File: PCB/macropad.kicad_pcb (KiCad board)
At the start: 2 copper layers, 83.5 x 97.3 mm, 40 parts, among them SW1 SW_Push, SW10 SW_Push, SW11 SW_Push, SW12 SW_Push, SW13 SW_Push, SW14 SW_Push, SW15 SW_Push, SW16 SW_Push, SW2 SW_Push, SW3 SW_Push, SW4 SW_Push, SW5 SW_Push, SW6 SW_Push, SW7 SW_Push, SW8 SW_Push, SW9 SW_Push, U2 MOUDLE-SEEEDUINO-XIAO

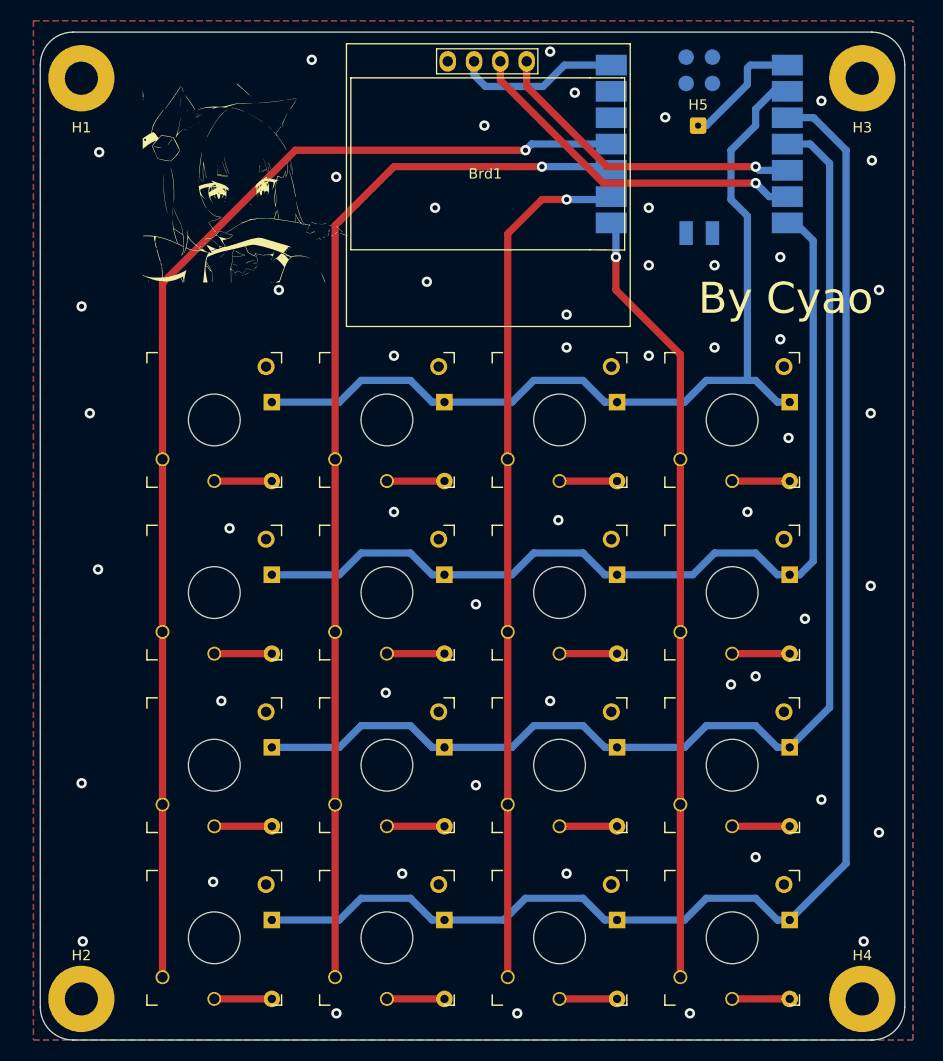
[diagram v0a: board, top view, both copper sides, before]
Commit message: Add pullup resistors for I2C
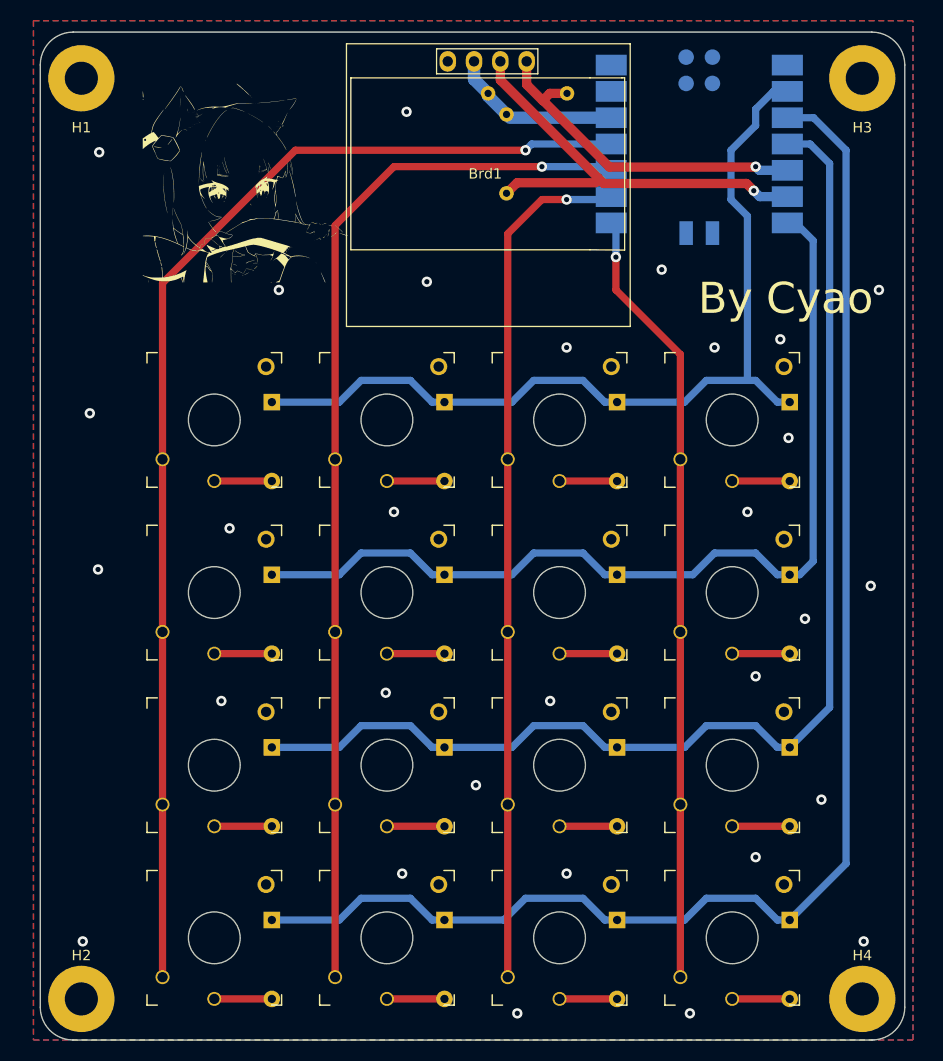
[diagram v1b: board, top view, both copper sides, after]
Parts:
- removed H5: MountingHole_Pad, Connector_Wire:SolderWire-0.1sqmm_1x01_D0.4mm_OD1mm
- added R1: R4.7, Resistor_THT:R_Axial_DIN0204_L3.6mm_D1.6mm_P7.62mm_Horizontal, B.Cu at (151.4, 57.5)
- added R2: R4.7, Resistor_THT:R_Axial_DIN0204_L3.6mm_D1.6mm_P7.62mm_Horizontal, B.Cu at (149.6, 55.4)
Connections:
- Brd1 pad 2: +5V -> +3.3V
- U2 pad 1: Net-(U2-PA02_A0_D0) -> unconnected-(U2-PA02_A0_D0-Pad1)
- U2 pad 12: +3V3 -> +3.3V
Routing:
- net +3.3V: track 0.00 -> 16.7 mm
- net +5V: track 15.9 -> 0.00 mm
- net Net-(U2-PA02_A0_D0): track 12.0 -> 0.00 mm
- net Net-(Brd1-SCL): track 34.6 -> 44.0 mm
- net Net-(Brd1-SDA): track 31.2 -> 33.7 mm
- net GND: vias 53 -> 30

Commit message: Moved diodes
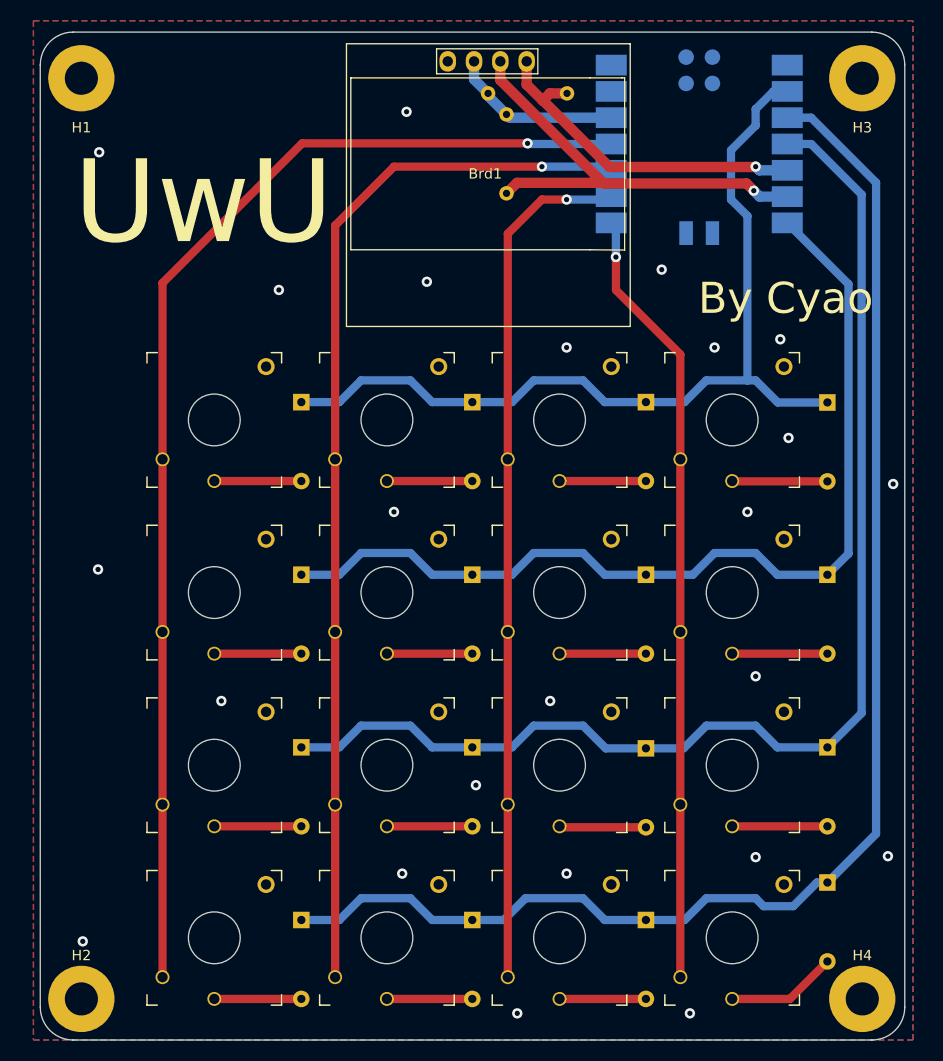
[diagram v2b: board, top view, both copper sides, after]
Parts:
- removed Gura!: LOGO, LOGO
- moved D13 5.13 mm to (182.4, 131.6)
- moved D10 3.64 mm to (182.4, 85.3)
- moved D11 3.64 mm to (182.4, 101.9)
- moved D12 3.64 mm to (182.4, 118.6)
- moved D1 2.85 mm to (131.6, 85.2)
- moved D16 2.85 mm to (131.6, 135.3)
- moved D4 2.85 mm to (131.6, 101.9)
- moved D7 2.85 mm to (131.6, 118.6)
- moved D9 2.79 mm to (164.8, 118.7)
- moved D14 2.78 mm to (164.8, 135.3)
- moved D3 2.78 mm to (164.8, 85.2)
- moved D6 2.78 mm to (164.8, 101.9)
- moved D15 2.69 mm to (148.1, 135.3)
- moved D2 2.69 mm to (148.1, 85.2)
- moved D5 2.69 mm to (148.1, 101.9)
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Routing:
- net Net-(D13-A): track 5.56 -> 10.7 mm
- net Net-(D10-A): track 5.56 -> 9.21 mm
- net Net-(D12-A): track 5.56 -> 9.20 mm
- net Net-(D11-A): track 5.56 -> 9.20 mm
- net Net-(D7-A): track 5.56 -> 8.40 mm
- net Net-(D4-A): track 5.56 -> 8.40 mm
- net Net-(D16-A): track 5.56 -> 8.40 mm
- net Net-(D1-A): track 5.56 -> 8.40 mm
- net Net-(D9-A): track 5.56 -> 8.38 mm
- net Net-(D6-A): track 5.56 -> 8.34 mm
- net Net-(D3-A): track 5.56 -> 8.34 mm
- net Net-(D14-A): track 5.56 -> 8.34 mm
- net Net-(D8-A): track 5.56 -> 8.25 mm
- net Net-(D5-A): track 5.56 -> 8.25 mm
- net Net-(D2-A): track 5.56 -> 8.25 mm
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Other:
- board text added: "UwU"

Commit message: Change side of tracks connecting to keys
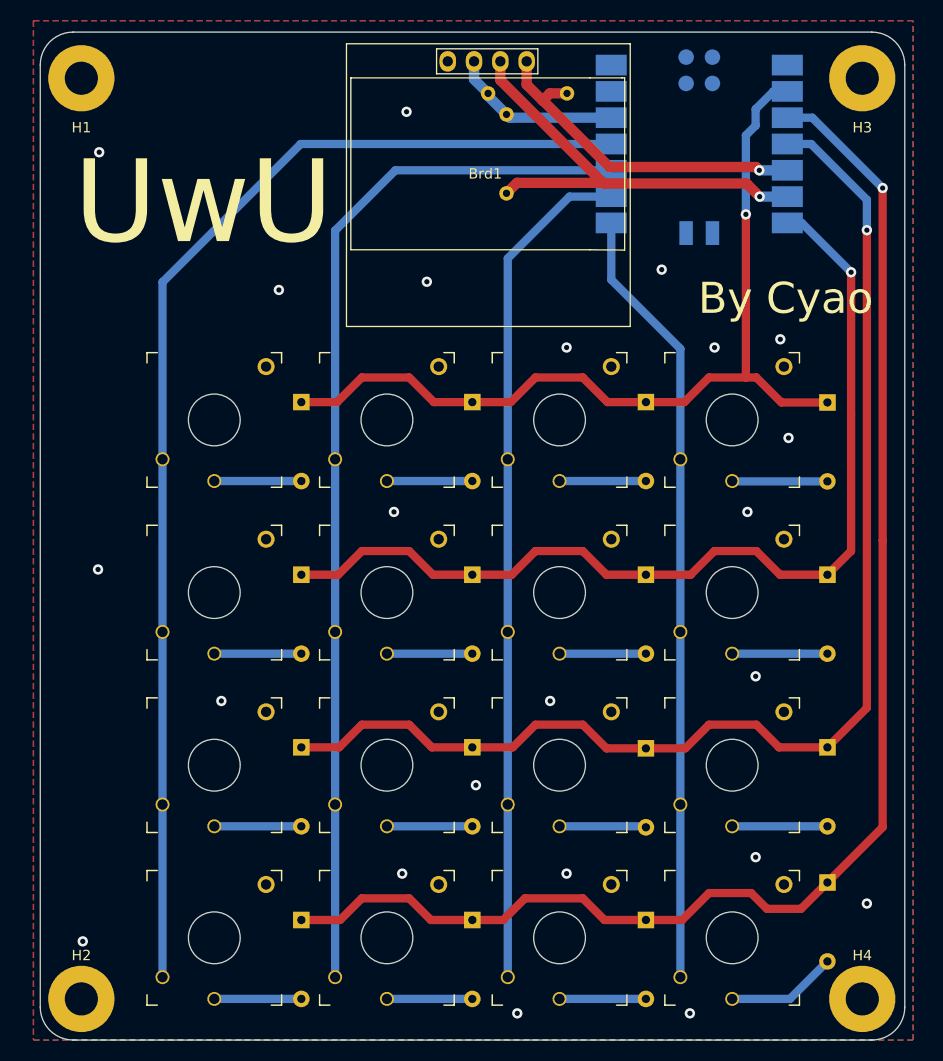
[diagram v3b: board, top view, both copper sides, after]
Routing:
- net ROW3: track 137.1 -> 138.3 mm, vias 0 -> 1
- net COL2: track 83.3 -> 82.3 mm, vias 1 -> 0
- net ROW0: track 87.6 -> 86.8 mm, vias 0 -> 1
- net ROW1: track 94.1 -> 94.8 mm, vias 0 -> 1
- net ROW2: track 120.0 -> 120.7 mm, vias 0 -> 1
- net COL3: track 75.6 -> 76.2 mm, vias 1 -> 0
- net COL1: vias 1 -> 0
- net COL0: vias 1 -> 0
- net GND: vias 24 -> 23

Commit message: Misc improvements
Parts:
- D1, D10, D11, D12, D13, D14, D15, D16, D2, D3, D4, D5, D6, D7, D8, D9: value D -> Didode 1N4148
- H1, H2, H3, H4: value MountingHole_Pad -> Mounting Hole
- R1, R2: value R4.7 -> Resistor 4.7k ohm
- SW1, SW10, SW11, SW12, SW13, SW14, SW15, SW16, SW2, SW3, SW4, SW5, SW6, SW7, SW8, SW9: value SW_Push -> Kailh Choc V2
- U2: value MOUDLE-SEEEDUINO-XIAO -> SEEEDUINO XIAO RP2040
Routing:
- net GND: vias 23 -> 22
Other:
- board text removed: "UwU"

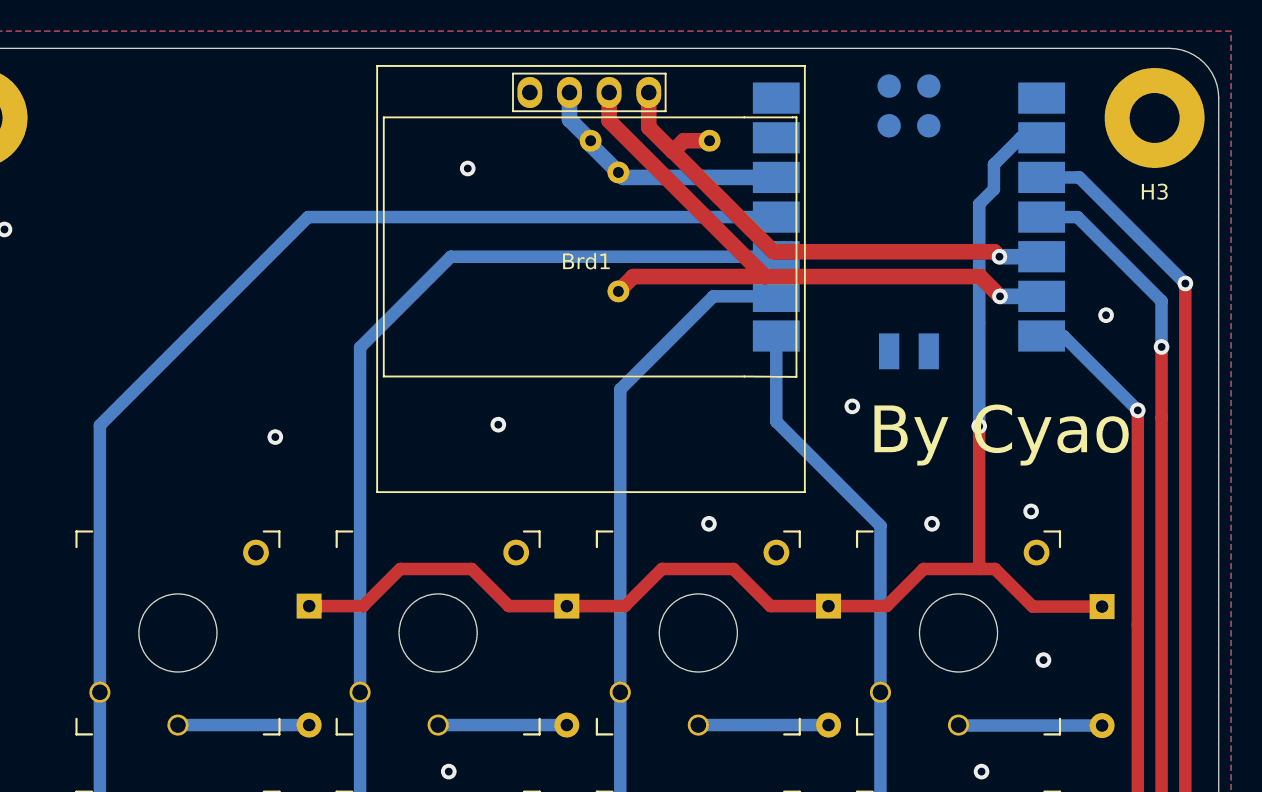
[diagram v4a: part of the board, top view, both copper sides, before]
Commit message: Use thru-hole xiao
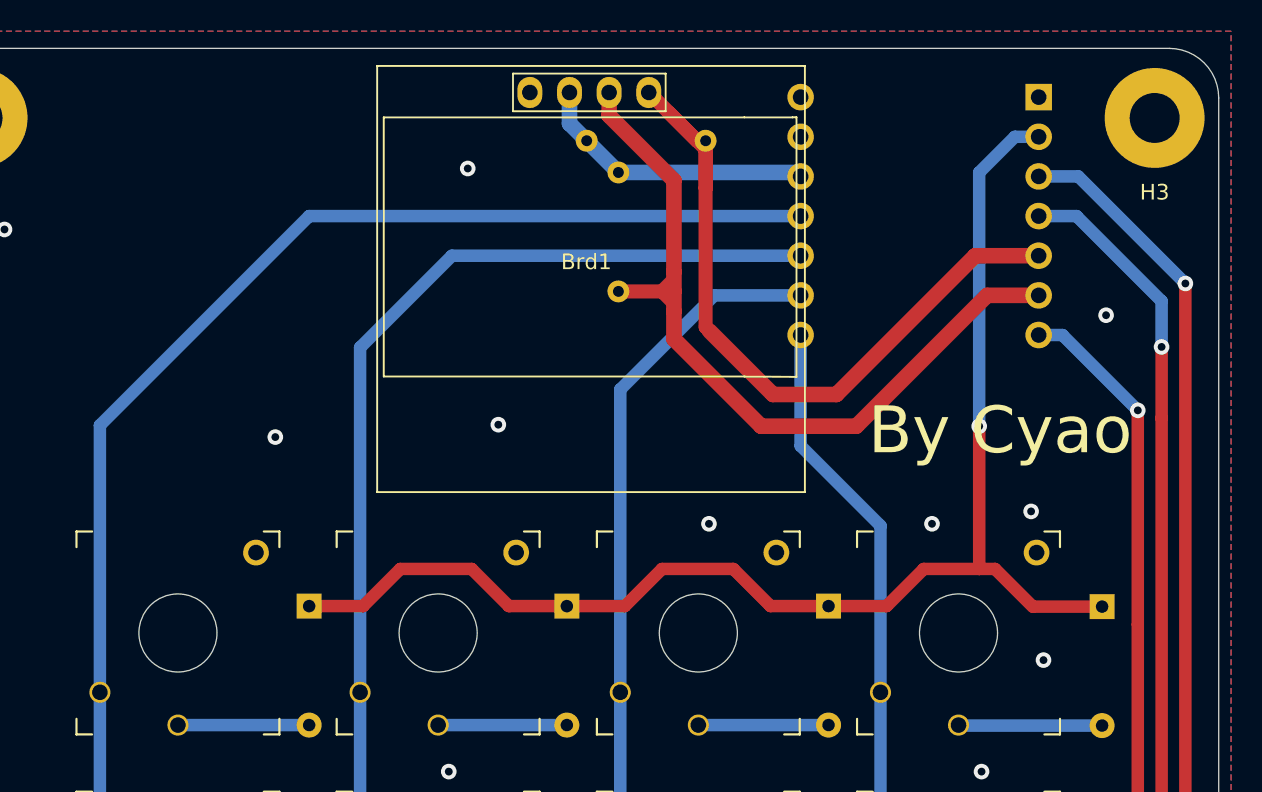
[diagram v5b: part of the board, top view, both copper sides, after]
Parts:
- U2: footprint seed:XIAO-SAMD21-RP2040-14P-2.54-21X17.8MM (Seeeduino XIAO) -> seed:XIAO-Generic-Thruhole-14P-2.54-21X17.8MM
- moved U2 0.69 mm to (170.7, 60.3)
- moved R2 0.25 mm to (149.4, 55.4)
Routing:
- net Net-(Brd1-SDA): track 33.6 -> 49.5 mm, vias 1 -> 0
- net Net-(Brd1-SCL): track 44.4 -> 52.5 mm, vias 1 -> 0
- net COL0: track 116.0 -> 117.6 mm
- net +3.3V: track 16.7 -> 18.2 mm
- net COL3: track 76.2 -> 75.0 mm
- net COL2: track 82.3 -> 83.5 mm
- net COL1: track 101.7 -> 102.8 mm
- net GND: vias 22 -> 21

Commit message: Redisigned PCB
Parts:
- removed H1, H2, H3, H4: Mounting Hole, MountingHole:MountingHole_3.2mm_M3_Pad
- R1, R2: value Resistor 4.7k ohm -> 4.7k
- moved R1 8.04 mm to (143.4, 58.3), turned to 0 degrees
- moved R2 5.96 mm to (143.4, 55.6)
- moved D13 5.43 mm to (177.8, 134.5)
- moved Brd1 4.89 mm to (144.4, 63.2)
- moved D12 4.66 mm to (177.8, 118.0)
- moved D11 4.64 mm to (177.8, 101.5)
- moved D10 4.63 mm to (177.8, 85.0)
- moved SW13 3.75 mm to (169.5, 136.2)
- moved SW12 3.72 mm to (169.5, 119.7)
- moved SW11 3.70 mm to (169.5, 103.2)
- moved SW10 3.68 mm to (169.5, 86.7)
- moved D14 3.68 mm to (161.2, 134.5)
- moved D9 3.66 mm to (161.2, 118.0)
- moved D6 3.62 mm to (161.2, 101.5)
- moved D3 3.61 mm to (161.2, 85.0)
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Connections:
- U2 pad 10: COL1 -> COL0
- U2 pad 11: COL0 -> COL3
- U2 pad 2: ROW0 -> ROW3
- U2 pad 3: ROW3 -> ROW2
- U2 pad 4: ROW2 -> ROW1
- U2 pad 7: ROW1 -> ROW0
- U2 pad 8: COL3 -> COL2
- U2 pad 9: COL2 -> COL1
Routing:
- net ROW0: track 87.0 -> 72.6 mm, vias 1 -> 0
- net COL1: track 102.8 -> 93.2 mm, vias 0 -> 1
- net COL3: track 75.0 -> 82.6 mm, vias 0 -> 1
- net ROW1: track 95.0 -> 101.4 mm, vias 1 -> 0
- net +3.3V: track 18.2 -> 24.5 mm
- net COL2: track 83.5 -> 77.5 mm, vias 0 -> 1
- net Net-(Brd1-SDA): track 49.5 -> 45.2 mm
- net ROW3: track 138.1 -> 142.4 mm, vias 1 -> 0
- net COL0: track 117.6 -> 114.2 mm, vias 0 -> 1
- net Net-(Brd1-SCL): track 52.5 -> 49.8 mm
- net Net-(D13-A): track 10.7 -> 8.25 mm
- net Net-(D10-A): track 9.21 -> 8.25 mm
- net Net-(D12-A): track 9.20 -> 8.25 mm
- net Net-(D11-A): track 9.20 -> 8.25 mm
- net ROW2: track 120.9 -> 121.5 mm, vias 1 -> 0
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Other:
- board size 83.5 x 97.3 mm -> 80.5 x 95.5 mm
- board text added: "Cyaopad"
- board text added: "Rev 4.0"
- board text removed: "By Cyao"
